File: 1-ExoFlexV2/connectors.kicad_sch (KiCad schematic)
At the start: 54 parts, among them J13 3, J14 3, J15 3, J16 5, J17 5, J18 5, J19 3, J20 3, J21 3, J22 3, J23 3, J24 3

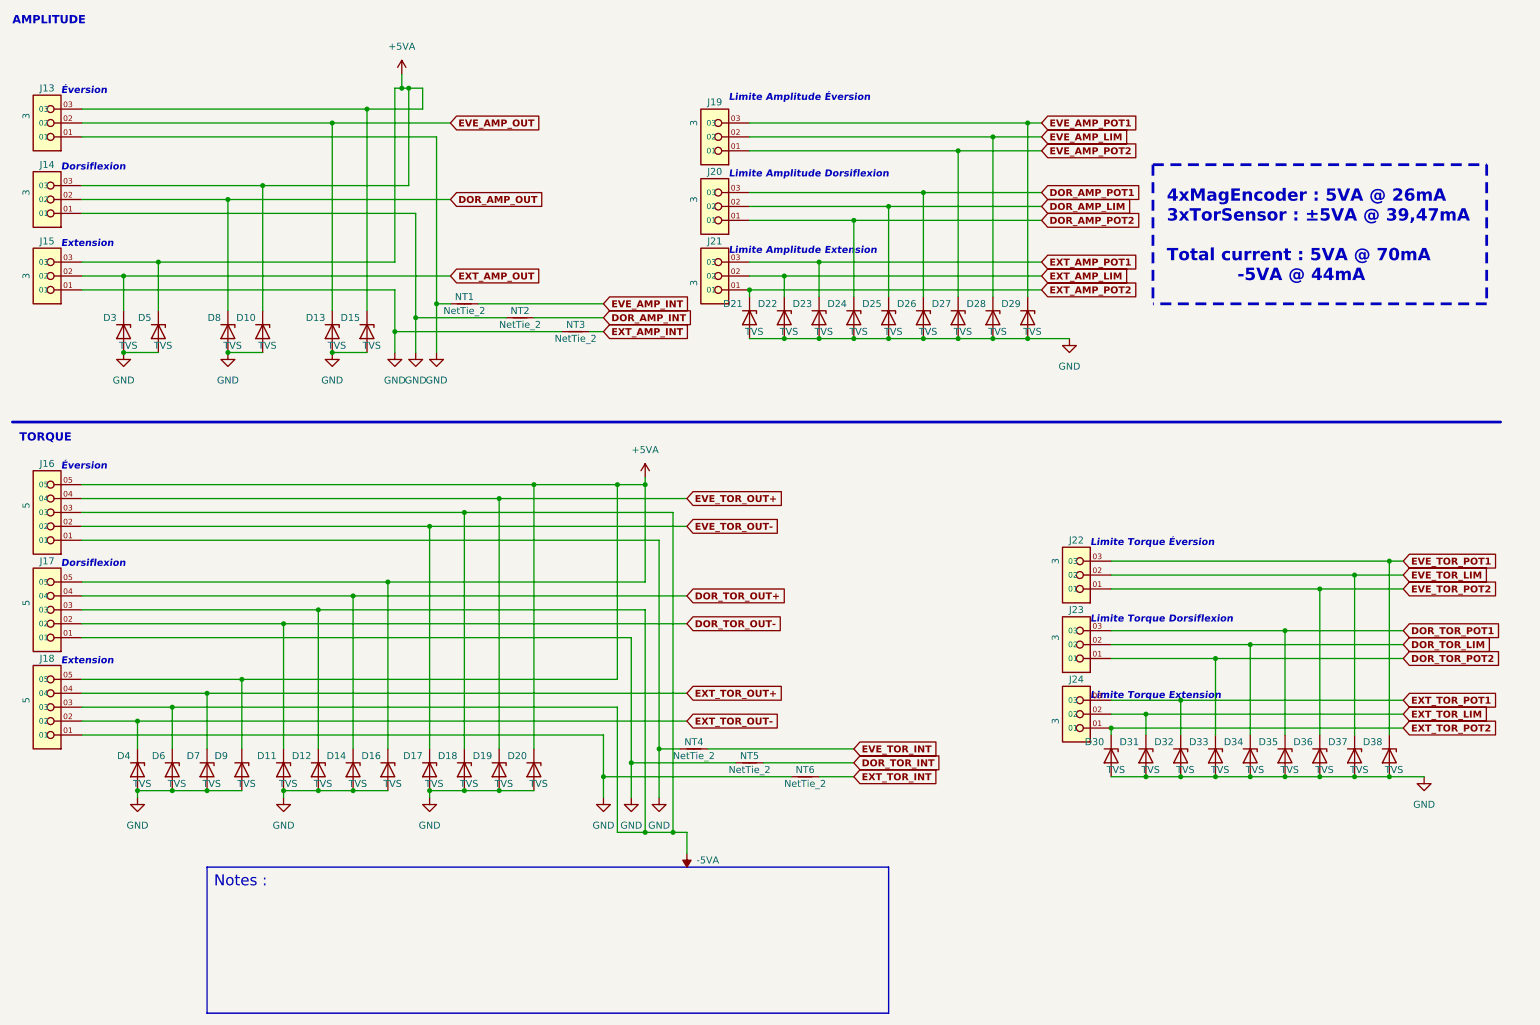
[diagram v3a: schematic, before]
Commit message: Finalisation 3
- Changement des régulateur de tension
- Retrait de test point inutile
- Changement de jumper mal positionner
- Ajout de Mounting holes et fiducial
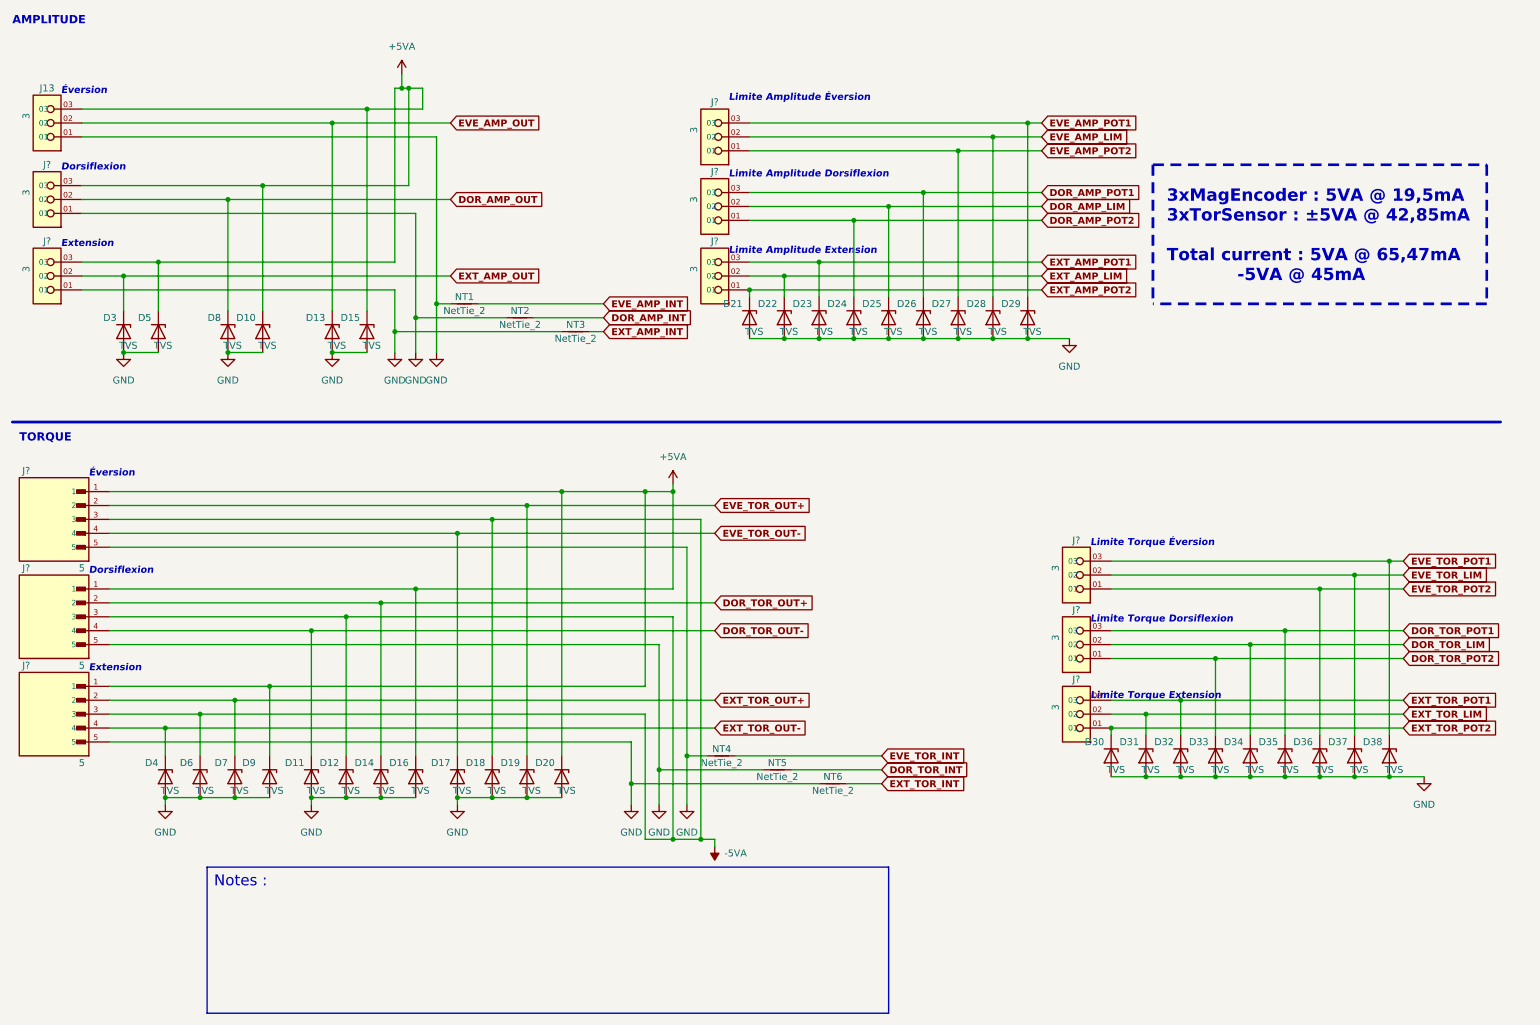
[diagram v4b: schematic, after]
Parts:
- removed J14, J15, J19, J20, J21, J22, J23, J24: 3, FootPrint:PHOENIX_1751109, symbol SymLib:1751109
- removed J16, J17, J18: 5, FootPrint:PHOENIX_1751125, symbol SymLib:1751125
- added J? (x8): 3, FootPrint:PHOENIX_1755749, symbol SymLib:1751109
- added J? (x3): 5, FootPrint:PHOENIX_1755765, symbol SymLib:1755765
- J13: footprint FootPrint:PHOENIX_1751109 -> FootPrint:PHOENIX_1755749; DESCRIPTION 3 Position Wire to Board Terminal Block 55° (125°) Angle wi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 -> 3 Position Terminal Block Header, Male Pins, Shrouded (4 Si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; PACKAGE 3 POS 0.100" (2.54mm) -> 3 POS 0.200" (5.08mm); PART NUMBER 1751109 -> 1755749
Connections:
- net +5VA: now also J?.03, J?.03, J?.1, J?.1, J?.1
- net -5VA: now also J?.3, J?.3, J?.3
- net DOR_AMP_LIM: now also J?.02
- net DOR_AMP_OUT: now also J?.02
- net DOR_AMP_POT1: now also J?.03
- net DOR_AMP_POT2: now also J?.01
- net DOR_TOR_LIM: now also J?.02
- net DOR_TOR_OUT+: now also J?.2
- net DOR_TOR_OUT-: now also J?.4
- net DOR_TOR_POT1: now also J?.03
- net DOR_TOR_POT2: now also J?.01
- net EVE_AMP_LIM: now also J?.02
- net EVE_AMP_POT1: now also J?.03
- net EVE_AMP_POT2: now also J?.01
- net EVE_TOR_LIM: now also J?.02
- net EVE_TOR_OUT+: now also J?.2
- net EVE_TOR_OUT-: now also J?.4
- net EVE_TOR_POT1: now also J?.03
- net EVE_TOR_POT2: now also J?.01
- net EXT_AMP_LIM: now also J?.02
- net EXT_AMP_OUT: now also J?.02
- net EXT_AMP_POT1: now also J?.03
- net EXT_AMP_POT2: now also J?.01
- net EXT_TOR_LIM: now also J?.02
- net EXT_TOR_OUT+: now also J?.2
- net EXT_TOR_OUT-: now also J?.4
- net EXT_TOR_POT1: now also J?.03
- net EXT_TOR_POT2: now also J?.01
- net GND: now also J?.01, J?.01, J?.5, J?.5, J?.5
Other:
- note added: "3xMagEncoder : 5VA @ 19,5mA 3xTorSensor : ±5VA @ 42,85mA Total current : 5VA @ 65,47mA -5VA @ 45mA"
- note removed: "4xMagEncoder : 5VA @ 26mA 3xTorSensor : ±5VA @ 39,47mA Total current : 5VA @ 70mA -5VA @ 44mA"
- moved on the sheet: D11, D12, D14, D16, D17, D18, D19, D20, D4, D6, D7, D9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

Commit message: Finalisation schéma FIN
- Changement des uméro pour les inverseurs
- Changement des connecteur et début de placement
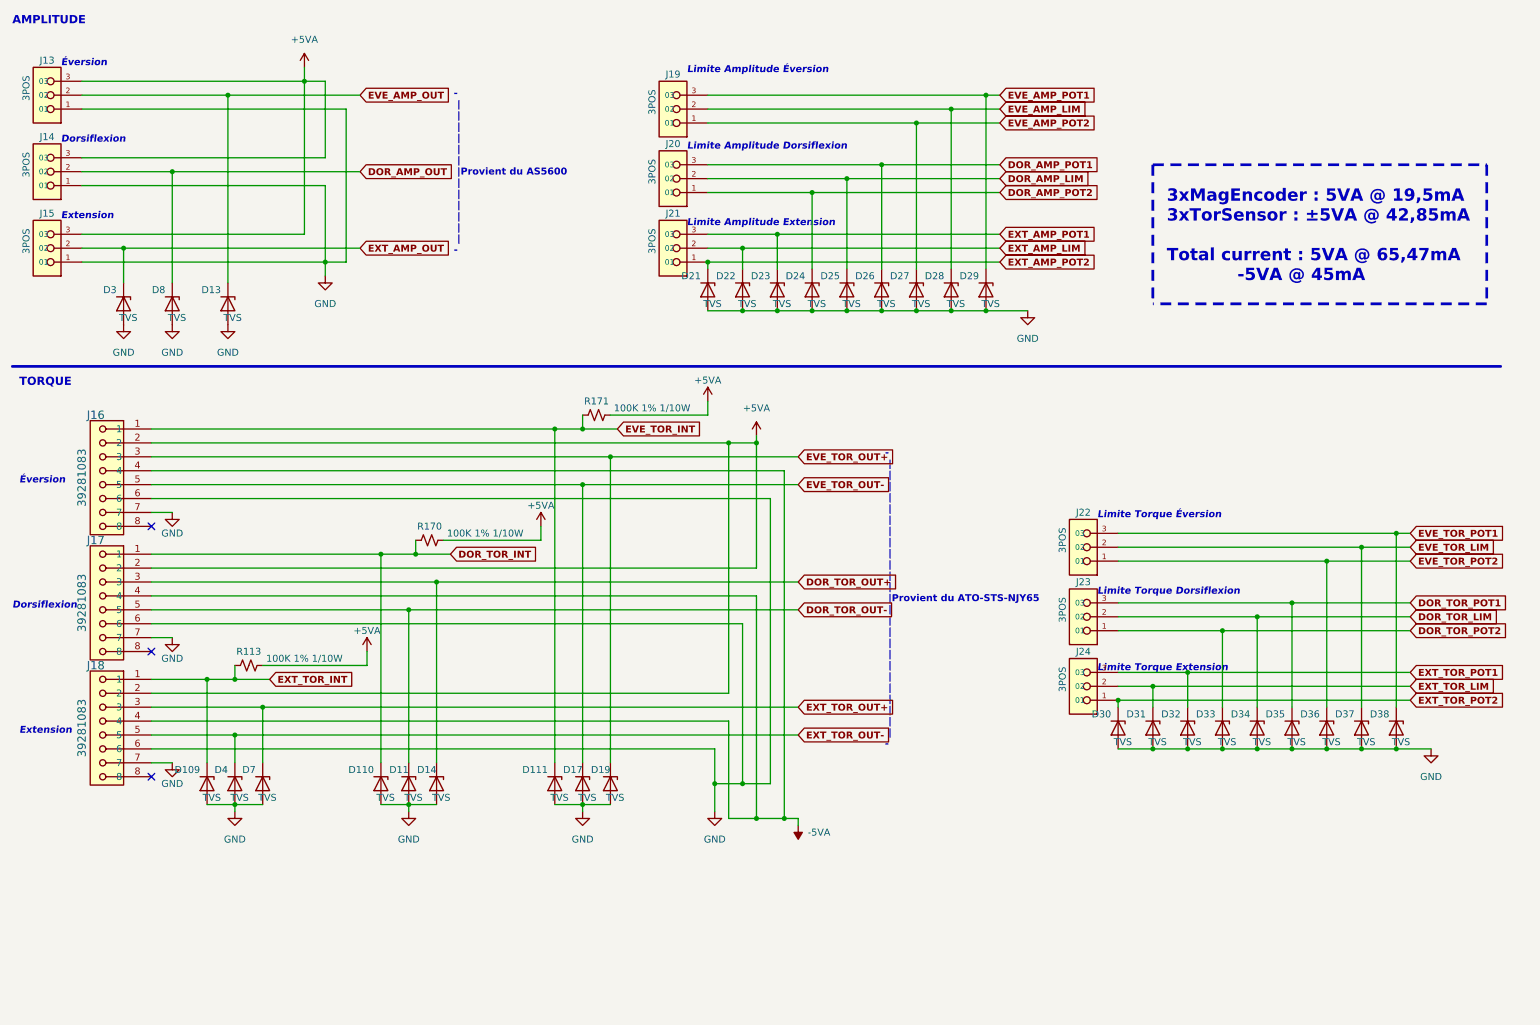
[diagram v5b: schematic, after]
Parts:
- removed D10, D12, D15, D16, D18, D20, D5, D6, D9: TVS, FootPrint:DPY2_TEX, symbol Device:D_Zener
- removed J? (x3): 5, FootPrint:PHOENIX_1755765, symbol SymLib:1755765
- removed NT1, NT2, NT3, NT4, NT5, NT6: NetTie_2, NetTie:NetTie-2_SMD_Pad0.5mm, symbol Device:NetTie_2
- added D109, D110, D111: TVS, FootPrint:DPY2_TEX, symbol Device:D_Zener
- added J16, J17, J18: 39281083, FootPrint:MOLEX_0039281083, symbol SymLib:39281083
- added R113, R170, R171: 100K 1% 1/10W, Resistor_SMD:R_0603_1608Metric, symbol Device:R_Small_US
- J13: value 3 -> 3POS; footprint FootPrint:PHOENIX_1755749 -> FootPrint:CON_39301039; DESCRIPTION 3 Position Terminal Block Header, Male Pins, Shrouded (4 Si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 -> Connector Header Through Hole 3 position 0.165" (4.20mm); MANUFACTURER Phoenix Contact -> Molex; PACKAGE 3 POS 0.200" (5.08mm) -> 3 POS 0.165" (4,2mm); PART NUMBER 1755749 -> 0039301039
- J14, J15, J19, J20, J21, J22, J23, J24: renamed from J?; value 3 -> 3POS; footprint FootPrint:PHOENIX_1755749 -> FootPrint:CON_39301039; DESCRIPTION 3 Position Terminal Block Header, Male Pins, Shrouded (4 Si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 -> Connector Header Through Hole 3 position 0.165" (4.20mm); MANUFACTURER Phoenix Contact -> Molex; PACKAGE 3 POS 0.200" (5.08mm) -> 3 POS 0.165" (4,2mm); PART NUMBER 1755749 -> 0039301039
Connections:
- net +5VA: now also J13.3 (03), J14.3 (03), J15.3 (03), J16.2, J17.2, J18.2, R113.2, R170.2, R171.2; no longer J13.03, J14.03, J15.03
- net -5VA: now also J16.4, J17.4, J18.4
- net DOR_AMP_LIM: now also J20.2 (02); no longer J20.02
- net DOR_AMP_OUT: now also J14.2 (02); no longer J14.02
- net DOR_AMP_POT1: now also J20.3 (03); no longer J20.03
- net DOR_AMP_POT2: now also J20.1 (01); no longer J20.01
- net DOR_TOR_INT: now also D110.1 (K), J17.1, R170.1
- net DOR_TOR_LIM: now also J23.2 (02); no longer J23.02
- net DOR_TOR_OUT+: now also J17.3
- net DOR_TOR_OUT-: now also J17.5
- net DOR_TOR_POT1: now also J23.3 (03); no longer J23.03
- net DOR_TOR_POT2: now also J23.1 (01); no longer J23.01
- net EVE_AMP_LIM: now also J19.2 (02); no longer J19.02
- net EVE_AMP_OUT: now also J13.2 (02); no longer J13.02
- net EVE_AMP_POT1: now also J19.3 (03); no longer J19.03
- net EVE_AMP_POT2: now also J19.1 (01); no longer J19.01
- net EVE_TOR_INT: now also D111.1 (K), J16.1, R171.1
- net EVE_TOR_LIM: now also J22.2 (02); no longer J22.02
- net EVE_TOR_OUT+: now also J16.3
- net EVE_TOR_OUT-: now also J16.5
- net EVE_TOR_POT1: now also J22.3 (03); no longer J22.03
- net EVE_TOR_POT2: now also J22.1 (01); no longer J22.01
- net EXT_AMP_LIM: now also J21.2 (02); no longer J21.02
- net EXT_AMP_OUT: now also J15.2 (02); no longer J15.02
- net EXT_AMP_POT1: now also J21.3 (03); no longer J21.03
- net EXT_AMP_POT2: now also J21.1 (01); no longer J21.01
- net EXT_TOR_INT: now also D109.1 (K), J18.1, R113.1
- net EXT_TOR_LIM: now also J24.2 (02); no longer J24.02
- net EXT_TOR_OUT+: now also J18.3
- net EXT_TOR_OUT-: now also J18.5
- net EXT_TOR_POT1: now also J24.3 (03); no longer J24.03
- net EXT_TOR_POT2: now also J24.1 (01); no longer J24.01
- net GND: now also J13.1 (01), J14.1 (01), J15.1 (01), D109.2 (A), D110.2 (A), D111.2 (A), J16.6, J16.7, J17.6, J17.7, J18.6, J18.7; no longer J13.01, J14.01, J15.01
- no-connect marks 0 -> 3
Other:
- note added: "- | | | | | | | | | | | | |Provient du ATO-STS-NJY65 | | | | | | | | | | | | -"
- note added: "- | | | | | | |Provient du AS5600 | | | | | | -"
- note removed: "Notes :"
- moved on the sheet: D11, D13, D14, D17, D19, D21, D22, D23, D24, D25, D26, D27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

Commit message: LAst changes
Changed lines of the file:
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@@
     (stroke (width 0) (type default) (color 0 0 0 0))
   )
-  (wire (pts (xy 38.1 104.14) (xy 41.91 104.14))
+  (wire (pts (xy 38.1 104.14) (xy 43.18 104.14))
     (stroke (width 0) (type default) (color 0 0 0 0))
   )
@@
     (pin "3")
   )
-  (symbol (lib_id "power:GND") (at 41.91 104.14 0) (unit 1)
-    (in_bom yes) (on_board yes)
-    (property "Reference" "#PWR0110" (id 0) (at 41.91 110.49 0)
-      (effects (font (size 1.27 1.27)) hide)
-    )
-    (property "Value" "GND" (id 1) (at 41.91 107.95 0))
-    (property "Footprint" "" (id 2) (at 41.91 104.14 0)
-      (effects (font (size 1.27 1.27)) hide)
-    )
-    (property "Datasheet" "" (id 3) (at 41.91 104.14 0)
-      (effects (font (size 1.27 1.27)) hide)
-    )
+  (symbol (lib_id "power:GND") (at 43.18 104.14 0) (unit 1)
+    (in_bom yes) (on_board yes)
+    (property "Reference" "#PWR0110" (id 0) (at 43.18 110.49 0)
+      (effects (font (size 1.27 1.27)) hide)
+    )
+    (property "Value" "GND" (id 1) (at 43.18 107.95 0))
+    (property "Footprint" "" (id 2) (at 43.18 104.14 0)
+      (effects (font (size 1.27 1.27)) hide)
+    )
+    (property "Datasheet" "" (id 3) (at 43.18 104.14 0)
+      (effects (font (size 1.27 1.27)) hide)
+    )
